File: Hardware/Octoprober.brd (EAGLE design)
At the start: 130.8 x 95 mm, 171 parts, among them J1 10118193-0001LF, SW1 EVQ-Q2203W, SW2 EVQ-Q2203W, SW3 EVQ-Q2203W, SW4 EVQ-Q2203W, SW5 EVQ-Q2203W, U1 P8X32A-M44, U10 DS1340Z-33+, U11 MCP3424-E/ST, U12 MCP3424-E/ST, U13 AT30TSE752-XM8-T, U14 AT30TSE752-XM8-T, U15 AT30TSE752-XM8-T, U16 AT30TSE752-XM8-T, U17 AT30TSE752-XM8-T, U18 AT30TSE752-XM8-T, U19 AT30TSE752-XM8-T, U2 CAT24C512WI-GT3, U20 AT30TSE752-XM8-T, U21 PMV22EN,215, U3 ADP3338AKCZ-3.3-RL, U4 FT230XQ-R, U5 BQ24075RGTT, U6 74HC2G04GV,125, U7 PMV22EN,215, U8 PMV160UP,215, U9 MCP3021A5T-E/OT, X1 ABLS3-6.000MHZ-D4Y-T, X2 ABS25-32.768KHz-1-T

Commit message: New chips for thermocouples.
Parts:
- removed C54: 1uF, PP_Passives:0402
- removed FU: (no value), PP_Connectors:HEADER_01X09_PTH
- removed J1: 10118193-0001LF, PP_Connectors:10118193-0001LF
- removed L10, L11, L12, L13, L14, L15, L16, L17, L3, L4, L5, L6, L7, L8, L9: BK1005HM471-T, PP_Passives:0402
- removed LCD1: (no value), PP_Displays:CHAR_DISPLAY_1602_COUNTERSINK
- removed R36: 10K, PP_Passives:0402
- removed R37, R38: 560, PP_Passives:0402
- removed U20: AT30TSE752-XM8-T, PP_DigitalIC:MSOP-8
- removed U21: PMV22EN,215, PP_DiscreteSemi:SOT-23
- added C55, C58, C59, C60, C63, C64, C65, C68, C69, C70, C73, C74: 0.1uF, PP_Passives:0402
- added C56, C57, C61, C62, C66, C67, C71, C72: 0.01uF, PP_Passives:0402
- added FID1: GSM_FIDUCIAL, MF_Aesthetics:GSM_FIDUCIAL
- added J3: (no value), MF_Connectors:MICROUSB-RIGHT
- added U$7: MF_LOGOLOGO_MEDIUM, PP_Aesthetics:MF_LOGO_MEDIUM
- C10, C11, C12, C13, C14, C2, C3, C34, C37, C38, C39, C4, C40, C5, C6, C9, R1, R10, R11, R12, R13, R14, R15, R16, R17, R18, R19, R20, R21, R22, R23, R24, R25, R26, R27, R28, R29, R30, R31, R32, R33, R34, R8, R9: device PP_Passives:0402 -> PP_Passives:0603
- C15, C21, C29, C49, C50: value 0.1uF -> 0.01uF
- C16, C18, C20, C24, C26, C28: value 0.01uF -> 0.1uF
- C17: value 10uF -> 0.01uF
- C19: value 10uF -> 0.1uF
- C41, C42, C43, C44: device PP_Passives:0402 -> PP_Passives:1206
- D1, D12, D2: device PP_LED:LED_0402 -> PP_LED:LED_0805
- L2: value BK1005HM471-T -> MI0603K300R-10; device PP_Passives:0402 -> PP_Passives:0603
- SD1: value 502570-0893 -> (none); device PP_Connectors:502570-0893 -> MF_Connectors:MICROSDSLOT-RIGHT
- U1: value P8X32A-M44 -> P8X32A-Q44; device PP_DigitalIC:QFN-44 -> MF_IC_Digital:LQFP44
- U11, U12: value MCP3424-E/ST -> MAX31856MUD+; device PP_DigitalIC:TTSOP-14 -> PP_AnalogIC:TTSOP-14
- U13, U14, U15, U16, U17, U18: value AT30TSE752-XM8-T -> MAX31856MUD+; device PP_DigitalIC:MSOP-8 -> PP_AnalogIC:TTSOP-14
- U19: value AT30TSE752-XM8-T -> IP4234CZ6,125; device PP_DigitalIC:MSOP-8 -> PP_Passives:SOT-457
- moved U1 241.2 mm to (-7.87, -155.2), turned to 0 degrees
- moved L2 232.3 mm to (1.52, -134.9), turned to 0 degrees
- moved U19 212.9 mm to (2.03, -124.0), turned to 0 degrees
- moved D8 197.6 mm to (1.52, -109.5), turned to 0 degrees
- moved U15 195.0 mm to (4.06, -97.8), turned to 0 degrees
- moved D9 194.8 mm to (7.62, -109.5), turned to 0 degrees
- moved U18 194.5 mm to (4.06, -104.4), turned to 0 degrees
- moved SD1 190.9 mm to (6.86, -149.9), turned to 0 degrees
- moved U16 190.2 mm to (12.4, -97.8), turned to 0 degrees
- moved TC5 187.3 mm to (1.27, -89.2), turned to 0 degrees
- moved U17 187.1 mm to (20.8, -97.8), turned to 0 degrees
- moved D10 186.9 mm to (9.91, -102.9), turned to 0 degrees
- moved D11 186.5 mm to (16.8, -102.9), turned to 0 degrees
- moved TC6 184.1 mm to (7.37, -89.2), turned to 0 degrees
- moved TC7 182.4 mm to (13.5, -89.2), turned to 0 degrees
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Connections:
- removed net LCD_CS: LCD1.16, U1.4
- removed net LCD_SDI: LCD1.14, U1.3
- removed net LCD_SDO: LCD1.13, U1.2
- removed net N$10: D6.2, L7.1, TC3.2
- removed net N$11: D6.1, L6.2, TC3.1
- removed net N$12: D7.2, L9.1, TC4.2
- removed net N$13: D7.1, L8.2, TC4.1
- removed net N$14: D11.2, L17.1, TC8.2
- removed net N$15: D11.1, L16.2, TC8.1
- removed net N$16: D10.2, L15.1, TC7.2
- removed net N$17: D10.1, L14.2, TC7.1
- removed net N$18: D9.2, L13.1, TC6.2
- removed net N$19: D9.1, L12.2, TC6.1
- removed net N$2: D4.2, L2.1, TC1.2
- removed net N$20: D8.2, L11.1, TC5.2
- removed net N$21: D8.1, L10.2, TC5.1
- removed net N$28: R37.1, U21.3
- removed net N$7: D4.1, L3.2, TC1.1
- removed net N$8: D5.2, L5.1, TC2.2
- removed net N$9: D5.1, L4.2, TC2.1
- removed net P12: FU.3, U1.13
- removed net P13: FU.4, U1.14
- removed net P14: FU.5, U1.15
- removed net P15: FU.6, U1.16
- removed net P16: FU.7, U1.19
- removed net P17: FU.8, U1.20
- removed net P18: FU.9, U1.21
- removed net SCL_ADC: U1.10, U11.8, U12.8, U13.P$2, U14.P$2, U15.P$2, U16.P$2, U17.P$2, U18.P$2, U19.P$2, U20.P$2
- removed net SDA_ADC: U1.11, U11.7, U12.7, U13.P$1, U14.P$1, U15.P$1, U16.P$1, U17.P$1, U18.P$1, U19.P$1, U20.P$1
- removed net SHT_DRAIN: R36.1, U1.12, U21.1
- new net ADC_0_!CS: U1.13, U11.P$9
- new net ADC_1_!CS: U1.14, U12.P$9
- new net ADC_2_!CS: U1.15, U13.P$9
- new net ADC_3_!CS: U1.16, U14.P$9
- new net ADC_4_!CS: U1.19, U15.P$9
- new net ADC_5_!CS: U1.20, U16.P$9
- new net ADC_6_!CS: U1.21, U17.P$9
- new net ADC_7_!CS: U1.22, U18.P$9
- new net ADC_SCK: U1.12, U11.P$10, U12.P$10, U13.P$10, U14.P$10, U15.P$10, U16.P$10, U17.P$10, U18.P$10
- new net ADC_SDI: U1.10, U11.P$12, U12.P$12, U13.P$12, U14.P$12, U15.P$12, U16.P$12, U17.P$12, U18.P$12
- new net ADC_SDO: U1.11, U11.P$11, U12.P$11, U13.P$11, U14.P$11, U15.P$11, U16.P$11, U17.P$11, U18.P$11
- new net LCD_SDA: U1.2
- new net N$23: J3.2, U19.6
- new net N$26: J3.3, U19.1
- new net N$27: J3.S1, J3.S2, J3.S3, J3.S4, J3.S5, J3.S6, J3.S7, J3.S8, L2.1
- new net P6: U1.3
- new net P7: U1.4
- net !SLEEP: no longer U1.23
- net 3.3V: now also SD1.PIN4; no longer C54.2, FU.1, LCD1.2, R36.2, R37.2, R38.1, SD1.5
- net 3.3V_ANALOG: now also C18.1, C24.1, C26.1, C46.1, C47.1, C51.1, C52.1, C58.1, C59.1, C63.1, C64.1, C68.1, C69.1, C73.1, C74.1, U11.P$5, U11.P$8, U12.P$5, U12.P$8, U13.P$5, U14.P$5, U15.P$5, U16.P$5; no longer C15.1, C17.1, C21.1, C29.2, C46.2, C47.2, C48.2, C49.2, C50.2, C51.2, C52.2, U11.5, U12.10, U12.5, U12.9, U14.P$7, U15.P$6, U16.P$6, U16.P$7, U18.P$7, U19.P$5, U19.P$6, U19.P$8, U20.P$5, U20.P$6, U20.P$7, U20.P$8
- net CHARGING: now also U1.23; no longer U1.22
- net D+: now also U19.3; no longer J1.3
- net D-: now also U19.4; no longer J1.2
- net GND: now also C18.2, C22.2, C24.2, C26.2, C29.2, C30.2, C46.2, C47.2, C49.2, C50.2, C51.2, C52.2, C56.2, C57.2, C58.2, C59.2, C61.2, C62.2, C63.2, C64.2, C66.2, C67.2, C68.2, C69.2, C71.2, C72.2, C73.2, C74.2, J3.5, L2.2, SD1.G0, SD1.G1, SD1.PIN6, U11.P$1, U11.P$14, U12.P$1, U12.P$14, U13.P$1, U13.P$14, U14.P$1, U14.P$14, U15.P$1, U15.P$14, U16.P$1, U16.P$14, U17.P$1, U17.P$14, U18.P$1, U18.P$14, U19.2; no longer C29.1, C46.1, C47.1, C48.1, C49.1, C50.1, C51.1, C52.1, C54.1, FU.2, J1.5, J1.S1, J1.S2, J1.S3, J1.S4, LCD1.1, R38.2, SD1.3, SD1.SHIELD0, SD1.SHIELD1, SD1.SHIELD2, SD1.SHIELD3, U11.10, U11.6, U11.9, U12.6, U13.P$4, U13.P$5, U13.P$6, U13.P$7, U14.P$4, U14.P$5, U14.P$6, U15.P$4, U15.P$5, U15.P$7, U16.P$4, U16.P$5, U17.P$4, U17.P$6, U17.P$7, U18.P$4, U18.P$6, U19.P$4, U19.P$7, U20.P$4, U21.2
- net IRQ: now also SD1.PIN8; no longer SD1.1
- net LCD_SCL: no longer LCD1.12
- net SD_CS: now also SD1.PIN2; no longer SD1.7
- net SD_DI: now also SD1.PIN3; no longer SD1.6
- net SD_DO: now also SD1.PIN7; no longer SD1.2
- net SD_RW: now also SD1.PIN1; no longer SD1.8
- net SD_SCLK: now also SD1.PIN5; no longer SD1.4
- net TP_T+_0: now also C17.1, D4.1, TC1.1, U11.P$4; no longer L3.1, U11.1
- net TP_T+_1: now also C20.2, C22.1, D5.1, TC2.1, U12.P$4; no longer C18.2, L4.1, U11.3
- net TP_T+_2: now also C28.2, C30.1, D6.1, TC3.1, U13.P$4; no longer C20.2, L6.1, U11.11
- net TP_T+_3: now also C48.2, C50.1, D7.1, TC4.1, U14.P$4; no longer C22.2, L8.1, U11.13
- net TP_T+_4: now also C55.2, C57.1, D8.1, TC5.1, U15.P$4; no longer C24.2, L10.1, U12.1
- net TP_T+_5: now also C60.2, C62.1, D9.1, TC6.1, U16.P$4; no longer C26.2, L12.1, U12.3
- net TP_T+_6: now also C65.2, C67.1, D10.1, TC7.1, U17.P$4; no longer C28.2, L14.1, U12.11
- net TP_T+_7: now also C70.2, C72.1, D11.1, TC8.1, U18.P$4; no longer C30.2, L16.1, U12.13
- net TP_T-_0: now also C15.1, D4.2, TC1.2, U11.P$2, U11.P$3; no longer L2.2, U11.2
- net TP_T-_1: now also C20.1, C21.1, D5.2, TC2.2, U12.P$2, U12.P$3; no longer C18.1, L5.2, U11.4
- net TP_T-_2: now also C28.1, C29.1, D6.2, TC3.2, U13.P$2, U13.P$3; no longer C20.1, L7.2, U11.12
- net TP_T-_3: now also C48.1, C49.1, D7.2, TC4.2, U14.P$2, U14.P$3; no longer C22.1, L9.2, U11.14
- net TP_T-_4: now also C55.1, C56.1, D8.2, TC5.2, U15.P$2, U15.P$3; no longer C24.1, L11.2, U12.2
- net TP_T-_5: now also C60.1, C61.1, D9.2, TC6.2, U16.P$2, U16.P$3; no longer C26.1, L13.2, U12.4
- net TP_T-_6: now also C65.1, C66.1, D10.2, TC7.2, U17.P$2, U17.P$3; no longer C28.1, L15.2, U12.12
- net TP_T-_7: now also C70.1, C71.1, D11.2, TC8.2, U18.P$2, U18.P$3; no longer C30.1, L17.2, U12.14
- net USB_V0: now also J3.1, U19.5; no longer J1.1
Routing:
- net GND: track 288.6 -> 0.00 mm, vias 82 -> 0
- net USB_V1: track 241.3 -> 0.00 mm, vias 2 -> 0
- net SDA_ADC: track 235.8 -> 0.00 mm, vias 9 -> 0
- net SCL_ADC: track 218.9 -> 0.00 mm, vias 11 -> 0
- net !SLEEP: track 207.5 -> 0.00 mm, vias 3 -> 0
- net !PWREN: track 200.3 -> 0.00 mm, vias 2 -> 0
- net BCD_CHARGER: track 161.4 -> 0.00 mm, vias 3 -> 0
- net 3.3V: track 133.1 -> 0.00 mm, vias 34 -> 0
- net CHARGING: track 117.0 -> 0.00 mm, vias 2 -> 0
- net N$4: track 109.3 -> 0.00 mm
- net LCD_SCL: track 107.3 -> 0.00 mm, vias 1 -> 0
- net LCD_SDO: track 102.1 -> 0.00 mm, vias 1 -> 0
- net LCD_SDI: track 97.1 -> 0.00 mm, vias 1 -> 0
- net LCD_CS: track 89.6 -> 0.00 mm, vias 1 -> 0
- net TX: track 78.9 -> 0.00 mm
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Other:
- board size 130.8 x 95 mm -> 7.1 x 1.2 mm
- board text removed: "+"
- board text removed: "+V"
- board text removed: "-"
- board text removed: "GND"
- board text removed: "PWR"
- board text removed: "PWR_ON"
- board text removed: "RESET"
- board text removed: "TX/RX"

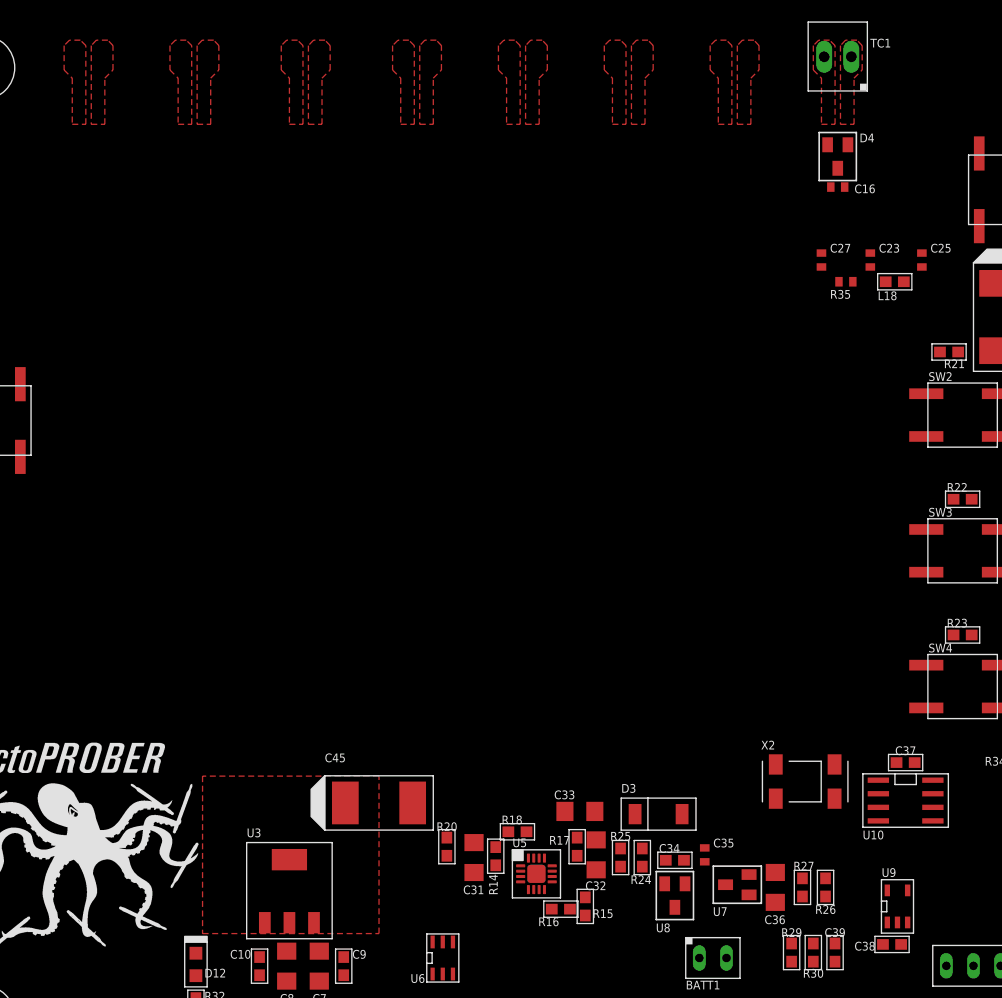
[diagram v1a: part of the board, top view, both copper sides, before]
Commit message: Working on LCD setup. Need to find a case.
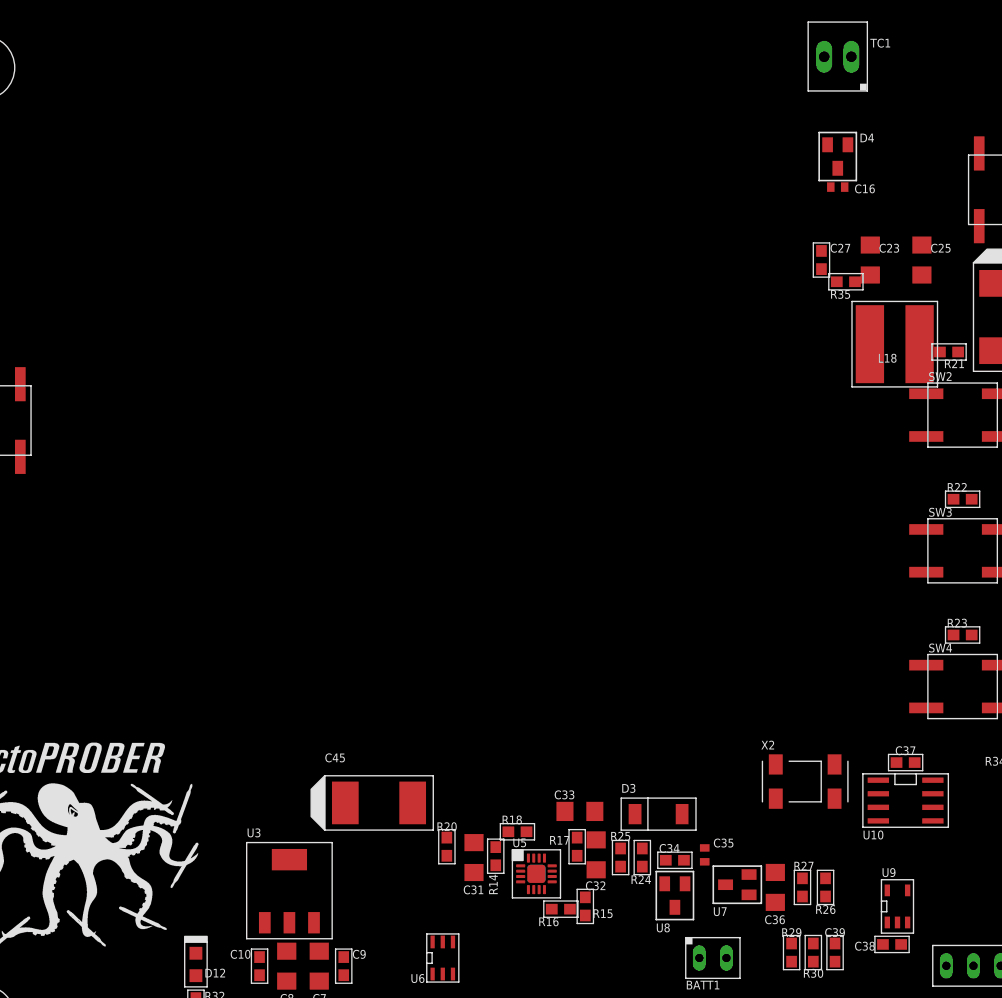
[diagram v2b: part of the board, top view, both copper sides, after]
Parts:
- C23, C25: device PP_Passives:0402 -> PP_Passives:1206
- C27, R35: device PP_Passives:0402 -> PP_Passives:0603
- L18: value LK1608100K-T -> CDRH6D28NP-100NC; device PP_Passives:0603 -> PP_Passives:CDRH6D28
- moved L18 5.84 mm to (88.4, 66.0)
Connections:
- net 3.3V: now also L18.P$2; no longer L18.2
- net N$25: now also L18.P$1; no longer L18.1
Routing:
- removed copper zone on layer 1, net 3.3V
- removed copper zone on layer 15, net 3.3V
- removed copper zone on layer 15, net 3.3V_ANALOG
- removed copper zone on layer 2, net GND
- removed copper zone on layer 1, net N$10
- removed copper zone on layer 1, net N$11
- removed copper zone on layer 1, net N$12
- removed copper zone on layer 1, net N$13
- removed copper zone on layer 1, net N$14
- removed copper zone on layer 1, net N$15
- removed copper zone on layer 1, net N$16
- removed copper zone on layer 1, net N$17
- removed copper zone on layer 1, net N$18
- removed copper zone on layer 1, net N$19
- removed copper zone on layer 1, net N$2
- removed copper zone on layer 1, net N$20
- removed copper zone on layer 1, net N$21
- removed copper zone on layer 1, net N$7
- removed copper zone on layer 1, net N$8
- removed copper zone on layer 1, net N$9

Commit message: Thermocouple connectors added.
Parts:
- removed TC1, TC2, TC3, TC4, TC5, TC6, TC7, TC8: 282834-2, PP_Connectors:HEADER_01X02_PTH_SCREWTERM
- added T1, T2, T3, T4, T5, T6, T7, T8: PCC-SMP-V, PP_Connectors:PCC-SMP-V
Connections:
- net TP_T+_0: now also T1.POS; no longer TC1.1
- net TP_T+_1: now also T2.POS; no longer TC2.1
- net TP_T+_2: now also T3.POS; no longer TC3.1
- net TP_T+_3: now also T4.POS; no longer TC4.1
- net TP_T+_4: now also T5.POS; no longer TC5.1
- net TP_T+_5: now also T6.POS; no longer TC6.1
- net TP_T+_6: now also T7.POS; no longer TC7.1
- net TP_T+_7: now also T8.POS; no longer TC8.1
- net TP_T-_0: now also T1.NEG; no longer TC1.2
- net TP_T-_1: now also T2.NEG; no longer TC2.2
- net TP_T-_2: now also T3.NEG; no longer TC3.2
- net TP_T-_3: now also T4.NEG; no longer TC4.2
- net TP_T-_4: now also T5.NEG; no longer TC5.2
- net TP_T-_5: now also T6.NEG; no longer TC6.2
- net TP_T-_6: now also T7.NEG; no longer TC7.2
- net TP_T-_7: now also T8.NEG; no longer TC8.2

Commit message: Switched display to a ERC128128FS
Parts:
- added C54: 10uF, PP_Passives:1206
- added C75: 0.01uF, PP_Passives:0603
- added C76, C77, C78, C79: 1uF, PP_Passives:0603
- added C80: 3.3uF, PP_Passives:0603
- added J1: ER-CON2.0-2P-SMD, PP_Connectors:ER-CON2.0-2P-SMD
- added J4: ER-CON31HT-1, PP_Connectors:ER-CON31HT-1
- added R36, R37: 22, PP_Passives:0603
- added R38, R39: 10K, PP_Passives:0603
- added U20: PMV160UP,215, PP_DiscreteSemi:SOT-23
- C15, C16, C17, C18, C19, C20, C21, C22, C24, C26, C28, C29, C30, C46, C47, C48, C49, C50, C51, C52, C55, C56, C57, C58, C59, C60, C61, C62, C63, C64, C65, C66, C67, C68, C69, C70, C71, C72, C73, C74: device PP_Passives:0402 -> PP_Passives:0603
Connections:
- removed net P6: U1.3
- removed net P7: U1.4
- new net A: J1.P$1, R36.2
- new net LCD_BKLT: R37.1, U1.4, U20.1
- new net LCD_RST: J4.P$5, U1.3
- new net N$10: C79.1, J4.P$27
- new net N$11: C78.1, J4.P$28
- new net N$12: C77.1, J4.P$29
- new net N$13: C76.1, J4.P$30
- new net N$14: C76.2, C77.2, C78.2, C79.2, C80.2
- new net N$2: C54.1, C75.1, J4.P$17, J4.P$18, J4.P$19, J4.P$20
- new net N$7: R36.1, U20.3
- new net N$8: C54.2, C75.2, J4.P$21, J4.P$22, J4.P$23, J4.P$24
- new net N$9: C80.1, J4.P$25
- net 3.3V: now also J4.P$10, J4.P$26, J4.P$3, J4.P$4, J4.P$6, J4.P$7, J4.P$8, J4.P$9, R37.2, R38.2, R39.2, U20.2
- net GND: now also J1.P$2, J4.P$1, J4.P$2
- net LCD_SCL: now also J4.P$11, J4.P$12, J4.P$13, J4.P$15, R38.1
- net LCD_SDA: now also J4.P$16, R39.1
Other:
- board size 7.1 x 1.2 mm -> 8.2 x 10.9 mm

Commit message: starting on the revamp.
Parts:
- removed BATT1: MIKROE-1120, PP_Connectors:HEADER_01X02_PTH
- removed FID1: GSM_FIDUCIAL, MF_Aesthetics:GSM_FIDUCIAL
- removed J2: (no value), PP_Connectors:HEADER_01X04_PTH
- removed U3: ADP3338AKCZ-3.3-RL, PP_PowerIC:SOT-223
- added J5: (no value), PP_Connectors:2.54MM_01X02_PIN_HEADER
- added J6: (no value), PP_Connectors:ER-CON2.0-2P-SMD
- added U21: 74HCT2G04GV,125, PP_DigitalIC:74HCT2G04_TTSOP-6
- J1: value ER-CON2.0-2P-SMD -> (none); device PP_Connectors:ER-CON2.0-2P-SMD -> PP_Connectors:2.54MM_01X04_PIN_HEADER
- OP1: device PP_DigitalIC:SOIC-8 -> PP_DigitalIC:ACPL-227_SO-8
- U10: value DS1340Z-33+ -> BQ24075RGTT; device PP_DigitalIC:SOIC-8 -> PP_PowerIC:BQ2407X_VQFN-16
- U11, U12, U13, U14, U15, U16, U17, U18: device PP_AnalogIC:TTSOP-14 -> PP_AnalogIC:MAX31856_TTSOP-14
- U19: device PP_Passives:SOT-457 -> PP_Passives:IP4234CZ6_SOT-457-6
- U2: device PP_DigitalIC:SOIC-8_W -> PP_DigitalIC:SOIC-8
- U20, U7, U8: device PP_DiscreteSemi:SOT-23 -> PP_DiscreteSemi:SOT-23-3
- U4: device PP_DigitalIC:QFN-16 -> PP_DigitalIC:FT230X_QFN-16
- U5: value BQ24075RGTT -> ADP3338AKCZ-3.3-RL; device PP_PowerIC:QFN-16_BOT_PAD -> PP_PowerIC:ADP3338_SOT-223-3
- U6: value 74HC2G04GV,125 -> DS1340Z-33+; device PP_DigitalIC:TTSOP-6 -> PP_DigitalIC:DS1340Z_SOIC-8
- U9: device PP_DigitalIC:SOT-23A -> PP_DigitalIC:MCP3021_SOT-23-5
- moved U2 366.6 mm to (-49.8, -290.1), turned to 0 degrees
- moved U10 356.8 mm to (-57.7, -301.8), turned to 0 degrees
- moved U5 338.2 mm to (-64.5, -300.0)
- moved U6 324.8 mm to (-49.8, -301.8)
- moved J1 50.3 mm to (-49.5, -276.6)
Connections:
- net !PWREN: now also U21.3; no longer U6.3
- net !SLEEP: now also U21.1; no longer U6.1
- net 3.3V: now also U21.5, U5.2, U5.PAD, U6.8; no longer U10.8, U3.COM1, U3.COM2, U6.5
- net A: now also J6.P$1; no longer J1.P$1
- net BCD_CHARGER: now also U10.5; no longer U5.5
- net CHARGING: now also U10.9; no longer U5.9
- net EXT_CON_0: now also J1.1; no longer J2.1
- net EXT_CON_1: now also J1.2; no longer J2.2
- net EXT_CON_2: now also J1.3; no longer J2.3
- net EXT_CON_3: now also J1.4; no longer J2.4
- net GND: now also J5.1, J6.P$2, U10.15, U10.8, U10.PAD0, U10.PAD1, U2.1, U21.2, U5.1, U6.4; no longer BATT1.1, J1.P$2, U10.4, U3.IN, U5.15, U5.8, U5.PAD0, U5.PAD1, U6.2
- net ILM: now also U10.12; no longer U5.12
- net ISET: now also U10.16; no longer U5.16
- net N$27: no longer J3.S7, J3.S8
- net PGOOD: now also U10.7; no longer U5.7
- net PWREN: now also U10.6, U21.4; no longer U5.6, U6.4
- net RTC_X1: now also U6.1; no longer U10.1
- net RTC_X2: now also U6.2; no longer U10.2
- net SCL: now also U6.6; no longer U10.6
- net SDA: now also U6.5; no longer U10.5
- net SLEEP: now also U10.4, U21.6; no longer U5.4, U6.6
- net SYS_V: now also U10.10, U10.11, U6.3; no longer U10.3, U5.10, U5.11
- net SYS_V_SW: now also U5.3; no longer U3.OUT
- net TS: now also U10.1; no longer U5.1
- net USB_V1: now also U10.13; no longer U5.13
- net VBATT: now also J5.2, U10.2, U10.3; no longer BATT1.2, U5.2, U5.3
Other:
- board outline removed
